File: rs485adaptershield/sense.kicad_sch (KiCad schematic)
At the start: 4 parts, among them U9 INA219AxD

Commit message: more work
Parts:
- removed C10: 100n, Capacitor_SMD:C_0805_2012Metric, symbol Device:C
- removed R13: 10k, Resistor_SMD:R_0805_2012Metric, symbol Device:R
- removed U9: INA219AxD, Package_SO:SOIC-8_3.9x4.9mm_P1.27mm, symbol Sensor_Energy:INA219AxD
- added C18, C19: 100n, Capacitor_SMD:C_0603_1608Metric, symbol Device:C
- added U1: INA293B3, Package_TO_SOT_SMD:SOT-23-5, symbol Amplifier_Current:INA293B3
- R12: value 10k -> 33k; footprint Resistor_SMD:R_0805_2012Metric -> Resistor_SMD:R_0603_1608Metric
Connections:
- net GND: now also C18.1, C19.2, U1.2 (GND)
- net +5V: no longer names the net of R12.2
- net +5V: now also U1.1 (OUT)
- net SDA renamed V_DIFF
- net V_DIFF: now also C19.1
- new net +3.3V: C18.2, U1.3 (Vs)
- new net R_SENSE+: U1.4 (IN+)
- new net R_SENSE-: U1.5 (IN-)

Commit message: more progress
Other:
- note added: "will need some sort of filter for this"
- moved on the sheet: C18, C19, R12, U1

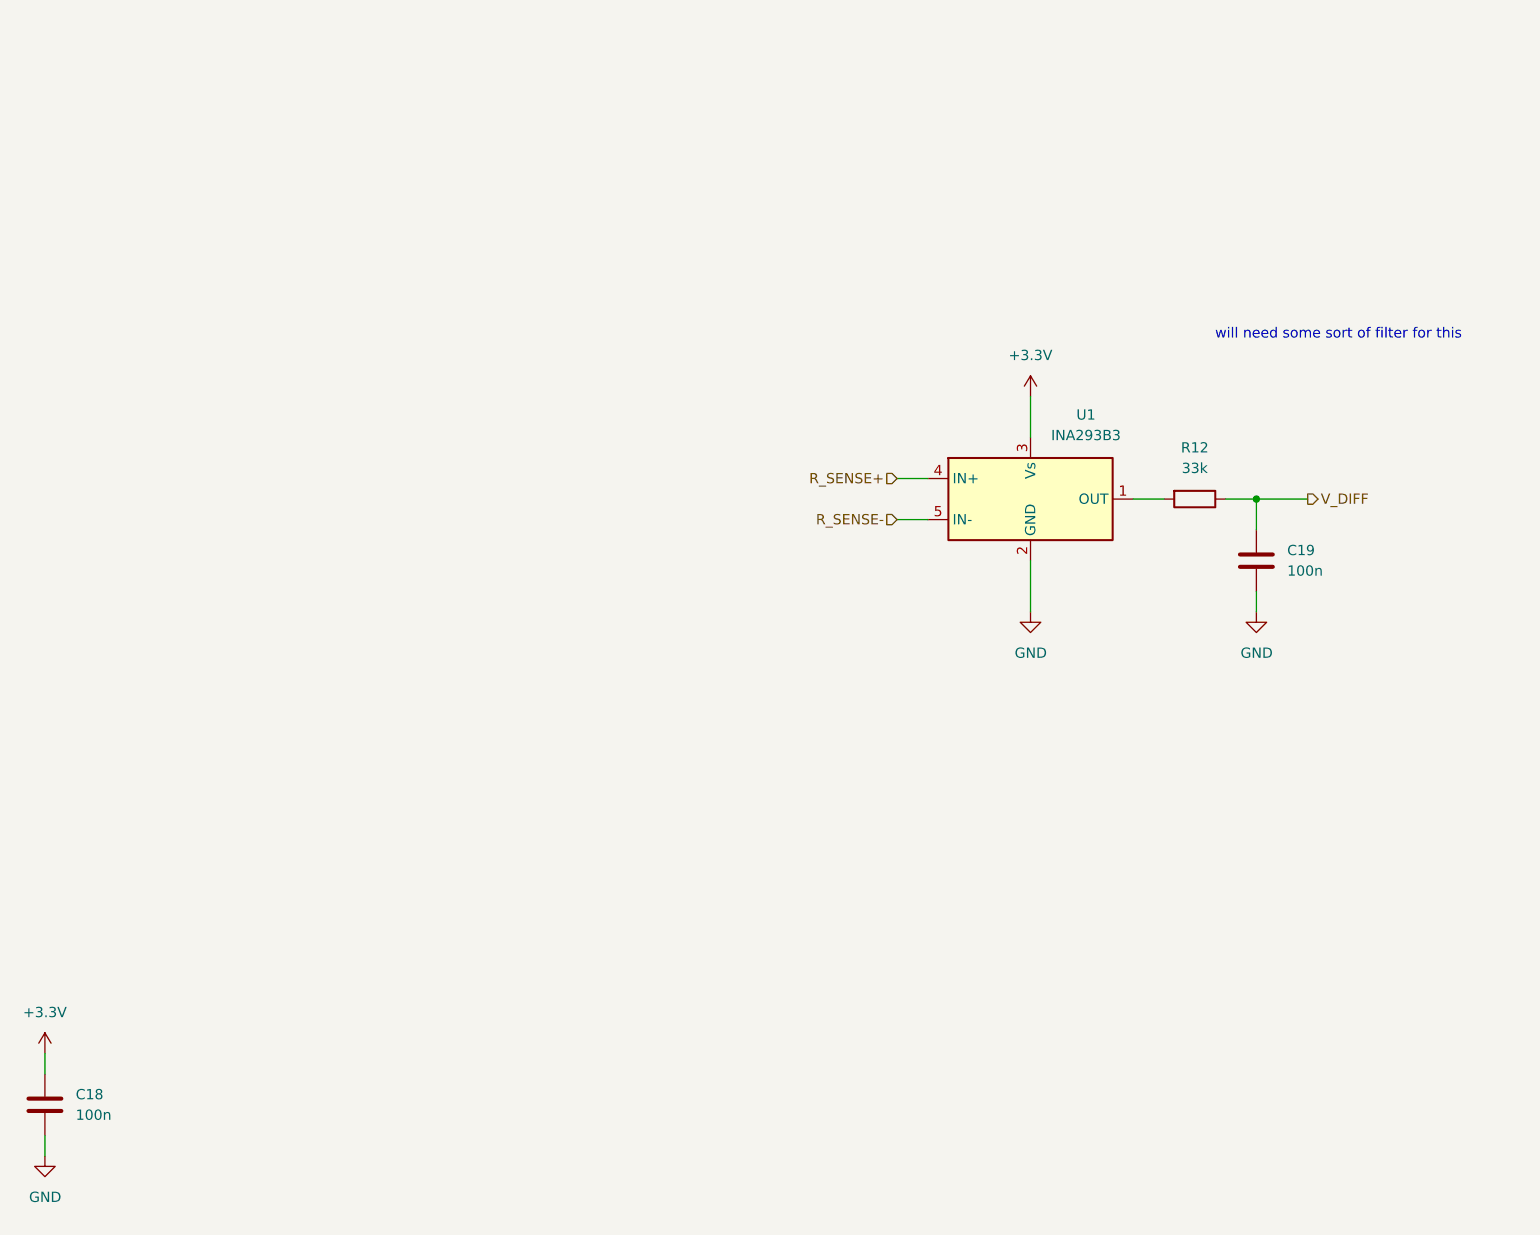
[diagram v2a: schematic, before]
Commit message: usb stackup problems
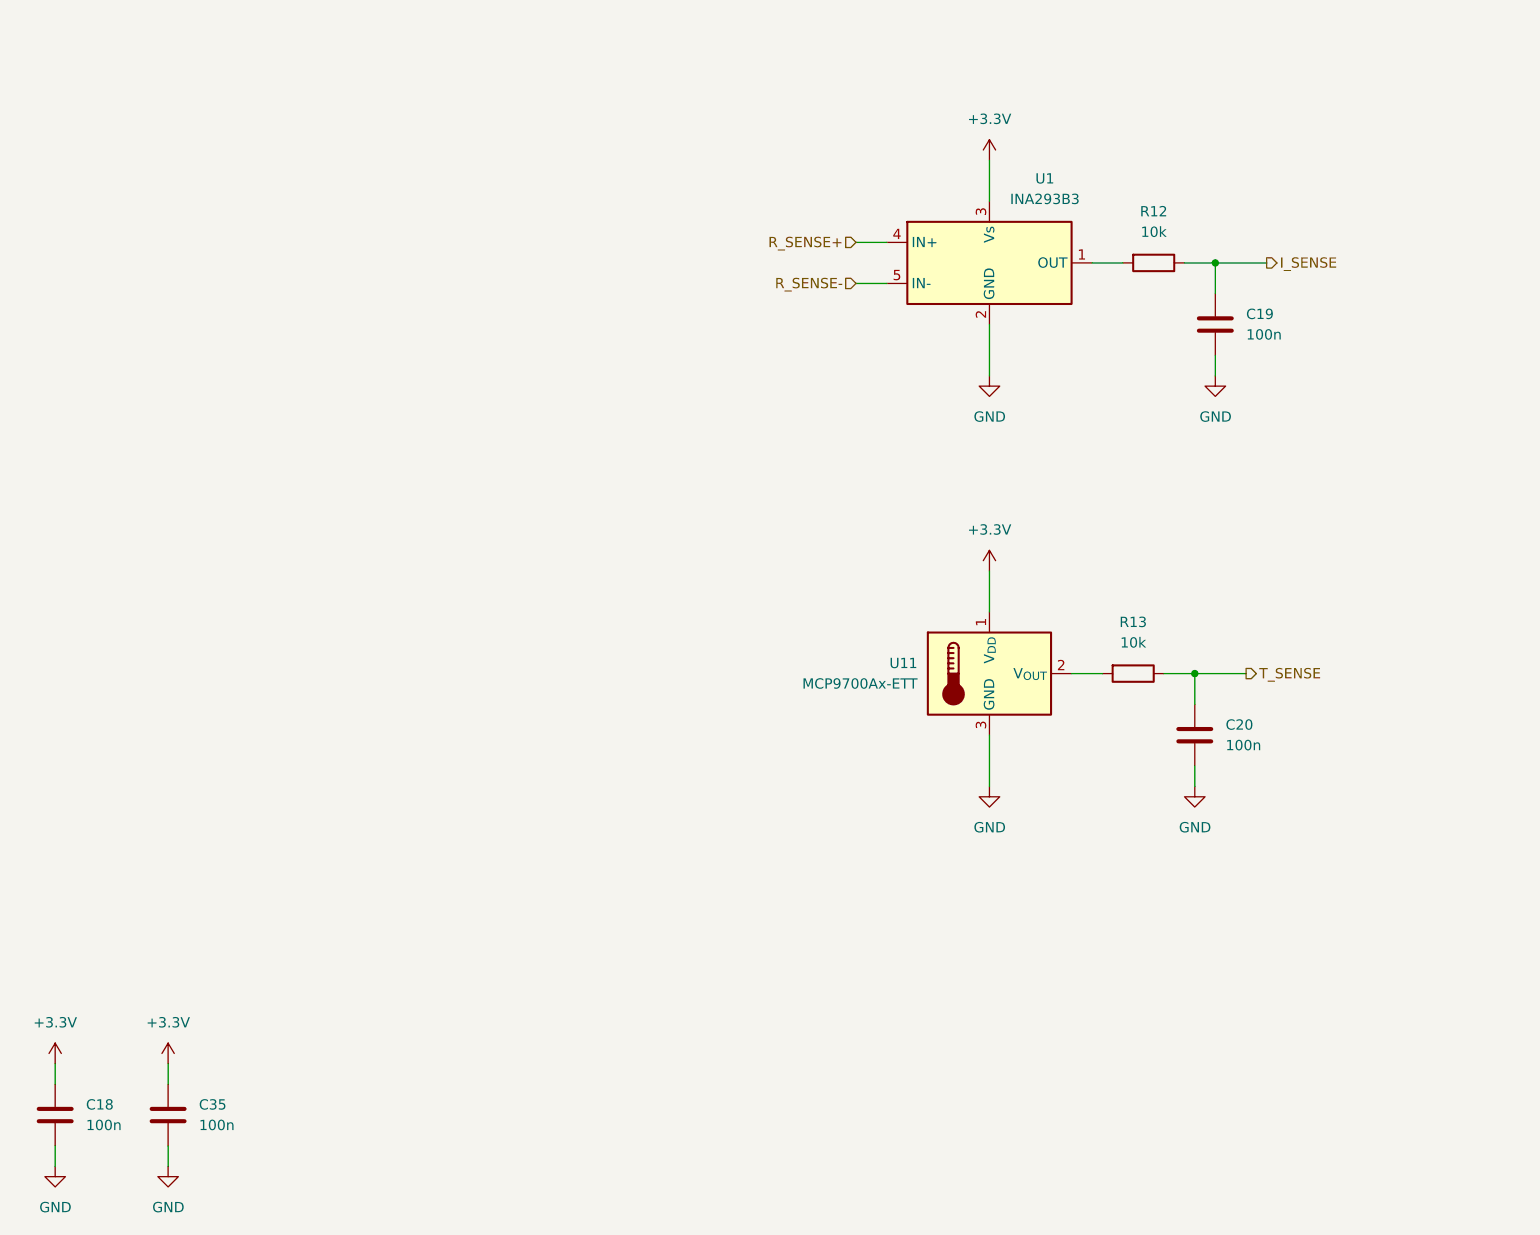
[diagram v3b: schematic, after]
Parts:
- added C20, C35: 100n, Capacitor_SMD:C_0402_1005Metric, symbol Device:C
- added R13: 10k, Resistor_SMD:R_0402_1005Metric, symbol Device:R
- added U11: MCP9700Ax-ETT, Package_TO_SOT_SMD:SOT-23, symbol Sensor_Temperature:MCP9700Ax-ETT
- C18, C19: footprint Capacitor_SMD:C_0603_1608Metric -> Capacitor_SMD:C_0402_1005Metric
- R12: value 33k -> 10k; footprint Resistor_SMD:R_0603_1608Metric -> Resistor_SMD:R_0402_1005Metric
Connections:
- net +3.3V: now also C35.2, U11.1 (V_{DD})
- net GND: now also C20.2, C35.1, U11.3 (GND)
- net V_DIFF renamed I_SENSE
- new net: R13.2, U11.2 (V_{OUT})
- new net T_SENSE: C20.1, R13.1
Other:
- note removed: "will need some sort of filter for this"
- moved on the sheet: C18, C19, R12, U1
